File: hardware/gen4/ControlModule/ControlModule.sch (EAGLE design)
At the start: 11 parts, among them IC1 XMEGA16A4A

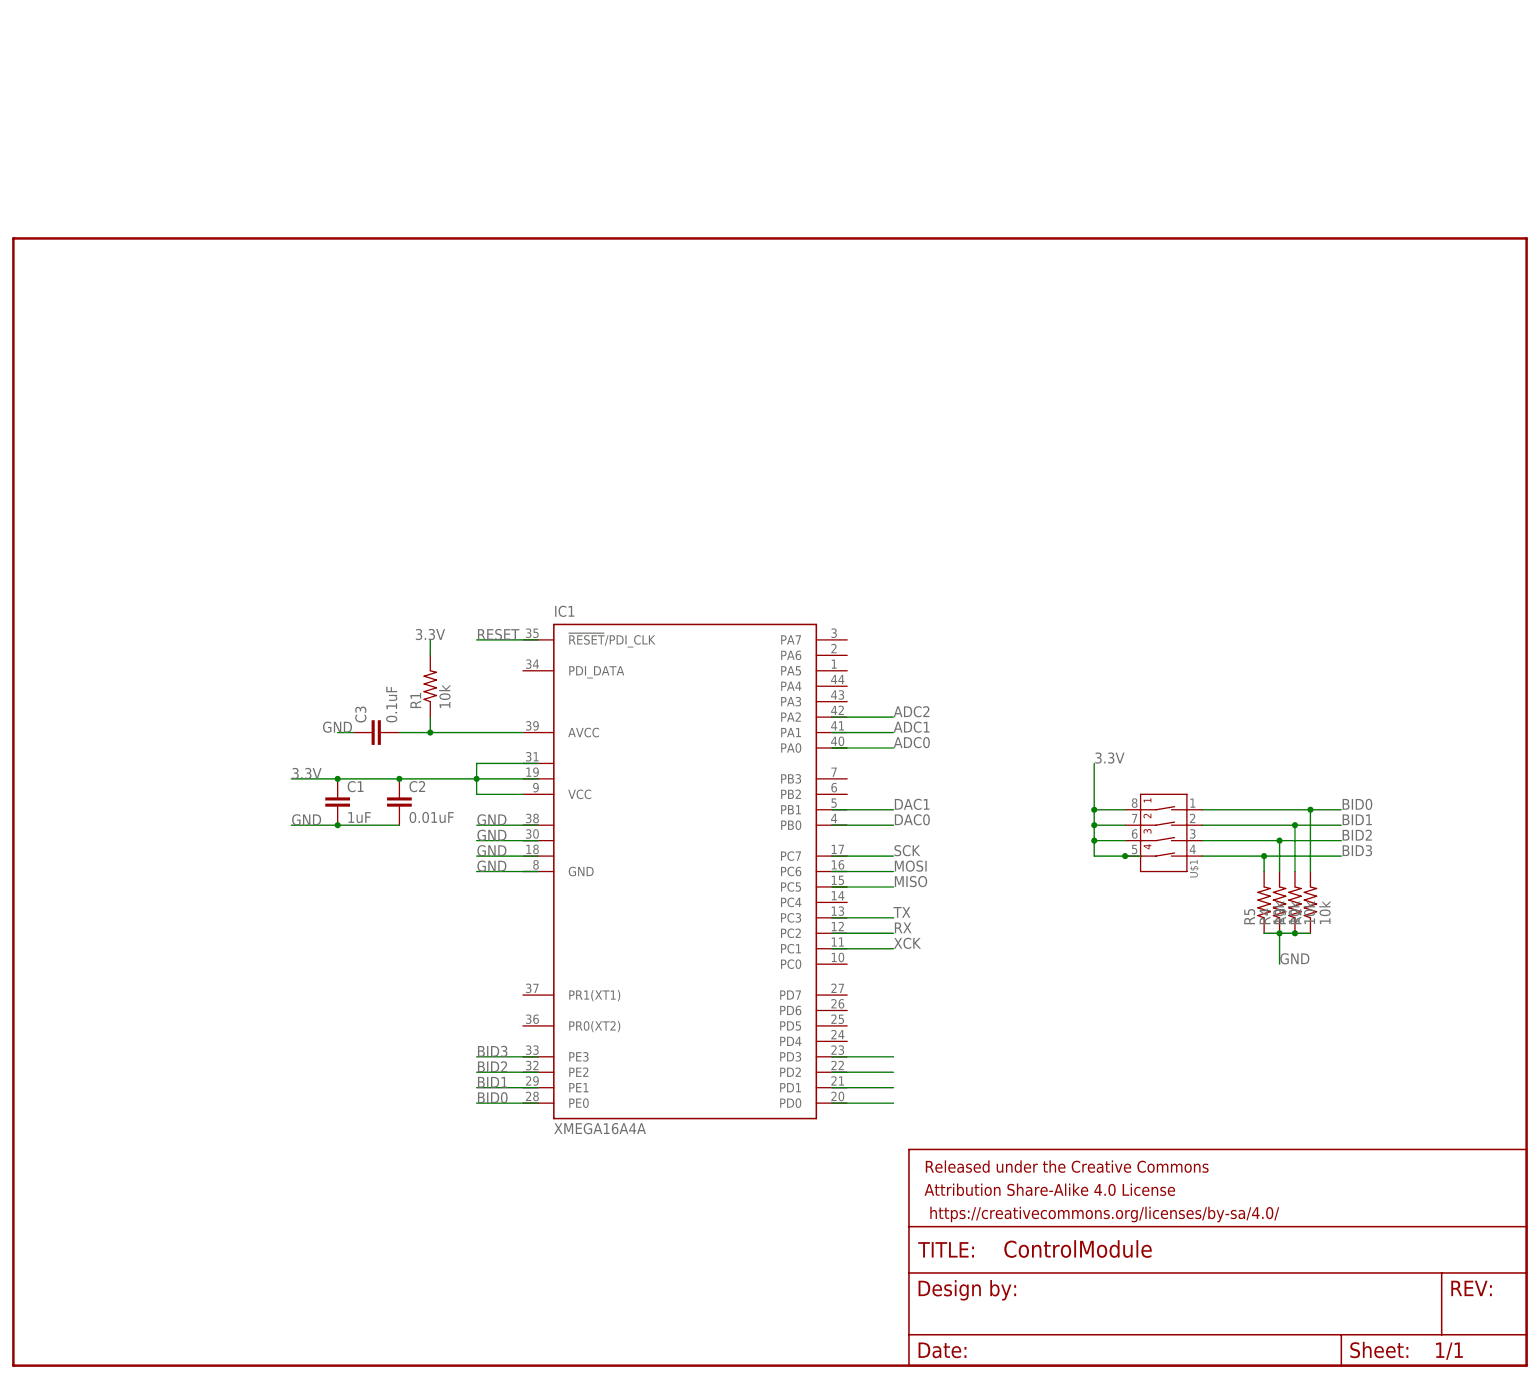
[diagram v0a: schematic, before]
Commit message: Added XBEE
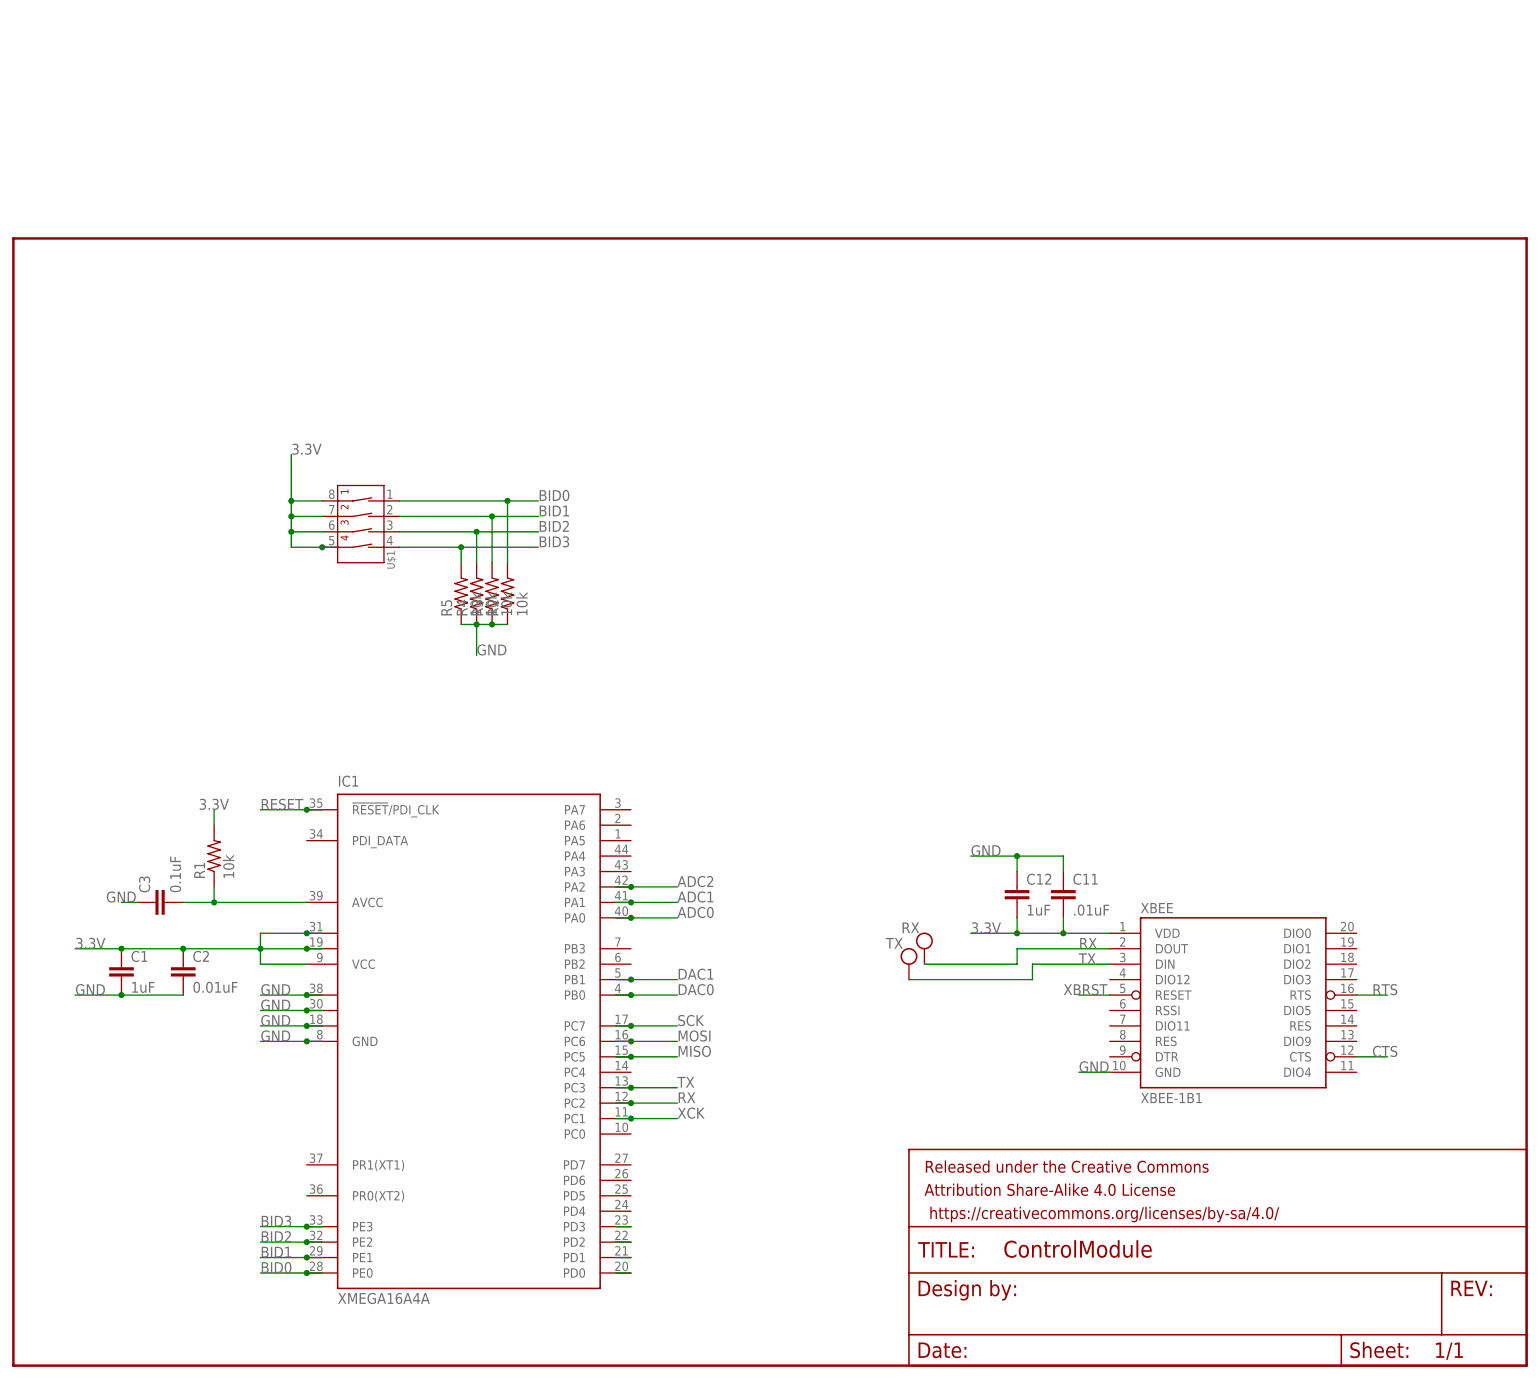
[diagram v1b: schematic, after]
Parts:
- added C11: .01uF, SparkFun-Capacitors:CAP0805
- added C12: 1uF, SparkFun-Capacitors:CAP0805
- added RX, TX: TEST_PT, gen3:TEST_PT
- added XBEE: XBEE-1B1, SparkFun-RF:XBEE-1B1
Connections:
- new net ADC0: IC1.PA0
- new net ADC1: IC1.PA1
- new net ADC2: IC1.PA2
- new net CTS: XBEE.CTS
- new net DAC0: IC1.PB0
- new net DAC1: IC1.PB1
- new net MISO: IC1.PC5
- new net MOSI: IC1.PC6
- new net N$2: IC1.PD0
- new net N$3: IC1.PD1
- new net N$4: IC1.PD2
- new net N$5: IC1.PD3
- new net RESET: IC1.!RESET!/PDI_CLK
- new net RTS: XBEE.RTS
- new net RX: IC1.PC2, RX.P$1, XBEE.DOUT
- new net SCK: IC1.PC7
- new net TX: IC1.PC3, TX.P$1, XBEE.DIN
- new net XBRST: XBEE.RESET
- new net XCK: IC1.PC1
- net 3.3V: now also C11.2, C12.2, IC1.VCC1, IC1.VCC2, XBEE.VDD
- net BID0: now also IC1.PE0
- net BID1: now also IC1.PE1
- net BID2: now also IC1.PE2
- net BID3: now also IC1.PE3
- net GND: now also C11.1, C12.1, IC1.GND, IC1.GND1, IC1.GND2, IC1.GND3, XBEE.GND
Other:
- moved on the sheet: C1, C2, C3, IC1, R1, R2, R3, R4, R5, U$1

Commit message: Working on xbee stuff for microboard
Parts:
- added R6: 4.7k, SparkFun-Passives:RESISTOR0805-RES
- added R7: 10k, SparkFun-Passives:RESISTOR0805-RES
- added R8: 80k, SparkFun-Passives:RESISTOR0805-RES
- added R9: 20k, SparkFun-Passives:RESISTOR0805-RES
- added S1, S2: SWITCH-MOMENTARY-2SMD-2, SparkFun-Electromechanical:SWITCH-MOMENTARY-2SMD-2
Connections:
- net ADC0 renamed BB_IN
- net ADC2 renamed DIVCAP
- net DAC0 renamed BB_OUT
- removed net ADC1: IC1.PA1
- removed net XCK: IC1.PC1
- new net 12V: R8.2
- new net BATSENSE: IC1.PA1, R8.1, R9.2
- net 3.3V: now also R7.2
- net GND: now also R9.1, S1.2, S2.1
- net N$5: now also R6.1
- net RESET: now also R7.1, S2.2
- net RX: no longer IC1.PC2
- net TX: no longer IC1.PC3
- net XBRST: now also R6.2, S1.1
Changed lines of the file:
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@@
 <part name="RX" library="gen3" deviceset="TEST_PT" device=""/>
 <part name="TX" library="gen3" deviceset="TEST_PT" device=""/>
+<part name="R6" library="SparkFun-Passives" deviceset="RESISTOR" device="0805-RES" value="4.7k"/>
+<part name="S1" library="SparkFun-Electromechanical" deviceset="SWITCH-MOMENTARY-2" device="SMD-2"/>
+<part name="S2" library="SparkFun-Electromechanical" deviceset="SWITCH-MOMENTARY-2" device="SMD-2"/>
+<part name="R7" library="SparkFun-Passives" deviceset="RESISTOR" device="0805-RES" value="10k"/>
+<part name="R8" library="SparkFun-Passives" deviceset="RESISTOR" device="0805-RES" value="80k"/>
+<part name="R9" library="SparkFun-Passives" deviceset="RESISTOR" device="0805-RES" value="20k"/>
 </parts>
 <sheets>
@@
 <instance part="RX" gate="G$1" x="149.86" y="68.58"/>
 <instance part="TX" gate="G$1" x="147.32" y="66.04"/>
+<instance part="R6" gate="G$1" x="119.38" y="22.86"/>
+<instance part="S1" gate="G$1" x="132.08" y="27.94" rot="R90"/>
+<instance part="S2" gate="G$1" x="27.94" y="101.6"/>
+<instance part="R7" gate="G$1" x="40.64" y="109.22" rot="R90"/>
+<instance part="R8" gate="G$1" x="127" y="83.82" rot="R90"/>
+<instance part="R9" gate="G$1" x="127" y="68.58" rot="R90"/>
 </instances>
 <busses>
@@
 </net>
 <net name="TX" class="0">
-<segment>
-<wire x1="99.06" y1="45.72" x2="101.6" y2="45.72" width="0.1524" layer="91"/>
-<label x="109.22" y="45.72" size="1.778" layer="95"/>
-<pinref part="IC1" gate="G$1" pin="PC3"/>
-<wire x1="101.6" y1="45.72" x2="109.22" y2="45.72" width="0.1524" layer="91"/>
-<junction x="101.6" y="45.72"/>
-</segment>
 <segment>
 <pinref part="XBEE" gate="G$1" pin="DIN"/>
@@
 <wire x1="167.64" y1="66.04" x2="180.34" y2="66.04" width="0.1524" layer="91"/>
 </segment>
+<segment>
+<wire x1="99.06" y1="33.02" x2="109.22" y2="33.02" width="0.1524" layer="91"/>
+<label x="109.22" y="33.02" size="1.778" layer="95"/>
+</segment>
 </net>
 <net name="RX" class="0">
-<segment>
-<wire x1="99.06" y1="43.18" x2="101.6" y2="43.18" width="0.1524" layer="91"/>
-<label x="109.22" y="43.18" size="1.778" layer="95"/>
-<pinref part="IC1" gate="G$1" pin="PC2"/>
-<wire x1="101.6" y1="43.18" x2="109.22" y2="43.18" width="0.1524" layer="91"/>
-<junction x="101.6" y="43.18"/>
-</segment>
 <segment>
 <pinref part="XBEE" gate="G$1" pin="DOUT"/>
@@
 <wire x1="165.1" y1="66.04" x2="149.86" y2="66.04" width="0.1524" layer="91"/>
 </segment>
-</net>
-<net name="XCK" class="0">
-<segment>
-<wire x1="99.06" y1="40.64" x2="101.6" y2="40.64" width="0.1524" layer="91"/>
-<label x="109.22" y="40.64" size="1.778" layer="95"/>
-<pinref part="IC1" gate="G$1" pin="PC1"/>
-<wire x1="101.6" y1="40.64" x2="109.22" y2="40.64" width="0.1524" layer="91"/>
-<junction x="101.6" y="40.64"/>
-</segment>
-</net>
-<net name="ADC0" class="0">
+<segment>
+<wire x1="99.06" y1="30.48" x2="109.22" y2="30.48" width="0.1524" layer="91"/>
+<label x="109.22" y="30.48" size="1.778" layer="95"/>
+</segment>
+</net>
+<net name="BB_IN" class="0">
 <segment>
 <wire x1="99.06" y1="73.66" x2="101.6" y2="73.66" width="0.1524" layer="91"/>
@@
 </segment>
 </net>
-<net name="ADC1" class="0">
+<net name="BATSENSE" class="0">
 <segment>
 <wire x1="99.06" y1="76.2" x2="101.6" y2="76.2" width="0.1524" layer="91"/>
 <label x="109.22" y="76.2" size="1.778" layer="95"/>
 <pinref part="IC1" gate="G$1" pin="PA1"/>
-<wire x1="101.6" y1="76.2" x2="109.22" y2="76.2" width="0.1524" layer="91"/>
 <junction x="101.6" y="76.2"/>
-</segment>
-</net>
-<net name="ADC2" class="0">
+<wire x1="101.6" y1="76.2" x2="127" y2="76.2" width="0.1524" layer="91"/>
+<wire x1="127" y1="76.2" x2="127" y2="73.66" width="0.1524" layer="91"/>
+<wire x1="127" y1="76.2" x2="127" y2="78.74" width="0.1524" layer="91"/>
+<junction x="127" y="76.2"/>
+<pinref part="R8" gate="G$1" pin="1"/>
+<pinref part="R9" gate="G$1" pin="2"/>
+</segment>
+</net>
+<net name="DIVCAP" class="0">
 <segment>
 <wire x1="99.06" y1="78.74" x2="101.6" y2="78.74" width="0.1524" layer="91"/>
@@
 <wire x1="48.26" y1="91.44" x2="40.64" y2="91.44" width="0.1524" layer="91"/>
 <junction x="48.26" y="91.44"/>
+<wire x1="40.64" y1="91.44" x2="40.64" y2="101.6" width="0.1524" layer="91"/>
+<wire x1="40.64" y1="101.6" x2="40.64" y2="104.14" width="0.1524" layer="91"/>
+<wire x1="40.64" y1="101.6" x2="33.02" y2="101.6" width="0.1524" layer="91"/>
+<junction x="40.64" y="101.6"/>
+<pinref part="S2" gate="G$1" pin="2"/>
+<pinref part="R7" gate="G$1" pin="1"/>
 </segment>
 </net>
@@
 <junction x="165.1" y="83.82"/>
 <label x="157.48" y="83.82" size="1.778" layer="95"/>
+</segment>
+<segment>
+<pinref part="S1" gate="G$1" pin="2"/>
+<wire x1="132.08" y1="33.02" x2="132.08" y2="40.64" width="0.1524" layer="91"/>
+<label x="132.08" y="40.64" size="1.778" layer="95" rot="R180"/>
+</segment>
+<segment>
+<pinref part="S2" gate="G$1" pin="1"/>
+<wire x1="22.86" y1="101.6" x2="17.78" y2="101.6" width="0.1524" layer="91"/>
+<label x="15.24" y="101.6" size="1.778" layer="95"/>
+</segment>
+<segment>
+<pinref part="R9" gate="G$1" pin="1"/>
+<wire x1="127" y1="63.5" x2="127" y2="60.96" width="0.1524" layer="91"/>
+<label x="127" y="60.96" size="1.778" layer="95"/>
 </segment>
 </net>
@@
 <junction x="172.72" y="71.12"/>
 </segment>
+<segment>
+<pinref part="R7" gate="G$1" pin="2"/>
+<wire x1="40.64" y1="114.3" x2="40.64" y2="116.84" width="0.1524" layer="91"/>
+<label x="40.64" y="116.84" size="1.778" layer="95"/>
+</segment>
 </net>
 <net name="N$1" class="0">
@@
 <wire x1="99.06" y1="22.86" x2="101.6" y2="22.86" width="0.1524" layer="91"/>
 <pinref part="IC1" gate="G$1" pin="PD3"/>
+<pinref part="R6" gate="G$1" pin="1"/>
+<wire x1="114.3" y1="22.86" x2="101.6" y2="22.86" width="0.1524" layer="91"/>
 </segment>
 </net>
@@
 </segment>
 </net>
-<net name="DAC0" class="0">
+<net name="BB_OUT" class="0">
 <segment>
 <wire x1="99.06" y1="60.96" x2="101.6" y2="60.96" width="0.1524" layer="91"/>
@@
 <label x="223.52" y="60.96" size="1.778" layer="95"/>
 </segment>
+<segment>
+<wire x1="99.06" y1="27.94" x2="109.22" y2="27.94" width="0.1524" layer="91"/>
+<label x="109.22" y="27.94" size="1.778" layer="95"/>
+</segment>
 </net>
 <net name="CTS" class="0">
@@
 <label x="223.52" y="50.8" size="1.778" layer="95"/>
 </segment>
+<segment>
+<wire x1="99.06" y1="25.4" x2="109.22" y2="25.4" width="0.1524" layer="91"/>
+<label x="109.22" y="25.4" size="1.778" layer="95"/>
+</segment>
 </net>
 <net name="XBRST" class="0">
@@
 <label x="172.72" y="60.96" size="1.778" layer="95"/>
 </segment>
-</net>
+<segment>
+<pinref part="R6" gate="G$1" pin="2"/>
+<pinref part="S1" gate="G$1" pin="1"/>
+<wire x1="124.46" y1="22.86" x2="132.08" y2="22.86" width="0.1524" layer="91"/>
+<wire x1="132.08" y1="22.86" x2="137.16" y2="22.86" width="0.1524" layer="91"/>
+<junction x="132.08" y="22.86"/>
+<label x="137.16" y="22.86" size="1.778" layer="95"/>
+</segment>
+</net>
+<net name="SCL" class="0">
+<segment>
+<wire x1="99.06" y1="40.64" x2="109.22" y2="40.64" width="0.1524" layer="91"/>
+<label x="109.22" y="40.64" size="1.778" layer="95"/>
+</segment>
+</net>
+<net name="SDA" class="0">
+<segment>
+<wire x1="99.06" y1="38.1" x2="109.22" y2="38.1" width="0.1524" layer="91"/>
+<label x="109.22" y="38.1" size="1.778" layer="95"/>
+</segment>
+</net>
+<net name="12V" class="0">
+<segment>
+<pinref part="R8" gate="G$1" pin="2"/>
+<wire x1="127" y1="88.9" x2="127" y2="91.44" width="0.1524" layer="91"/>
+<label x="127" y="91.44" size="1.778" layer="95"/>
+</segment>
+</net>
+<net name="SS_1" class="0">
+<segment>
+<wire x1="99.06" y1="91.44" x2="109.22" y2="91.44" width="0.1524" layer="91"/>
+<label x="109.22" y="91.44" size="1.778" layer="95"/>
+</segment>
+</net>
+<net name="SS_2" class="0">
+<segment>
+<wire x1="99.06" y1="88.9" x2="109.22" y2="88.9" width="0.1524" layer="91"/>
+<label x="109.22" y="88.9" size="1.778" layer="95"/>
+</segment>
+</net>
+<net name="SS_3" class="0">
+<segment>
+<wire x1="99.06" y1="86.36" x2="109.22" y2="86.36" width="0.1524" layer="91"/>
+<label x="109.22" y="86.36" size="1.778" layer="95"/>
+</segment>
+</net>
+<net name="SS_4" class="0">
+<segment>
+<wire x1="99.06" y1="83.82" x2="109.22" y2="83.82" width="0.1524" layer="91"/>
+<label x="109.22" y="83.82" size="1.778" layer="95"/>
+</segment>
+</net>
